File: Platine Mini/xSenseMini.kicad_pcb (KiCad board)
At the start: 2 copper layers, 30 x 20 mm, 25 parts, among them J1 Balancer, J2 Tele_Strom, J3 Serial_AIn, U1 SPX3819 3,3V, U2 ATmega328P-AU, U3 LM4040 2.5

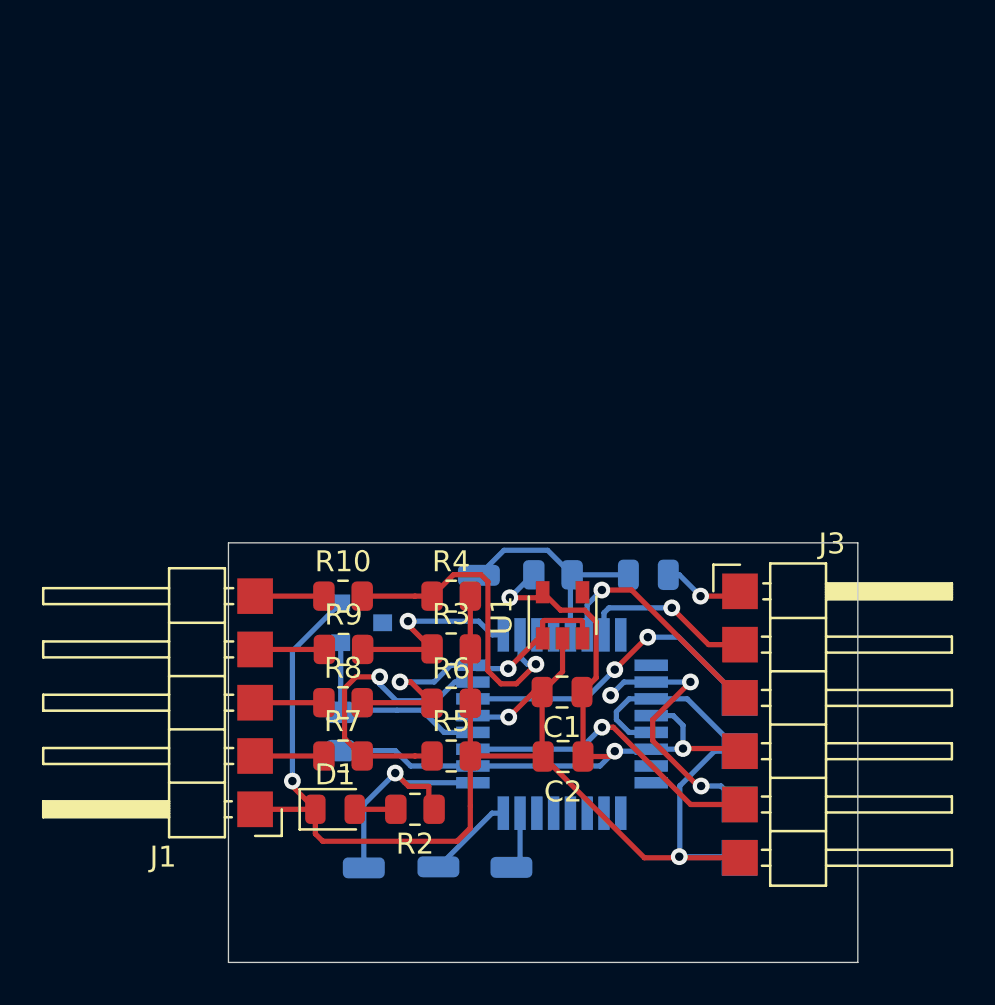
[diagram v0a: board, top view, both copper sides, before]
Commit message: + Schaltplan Mini Update + Komplett neu geroutet und finalisiert
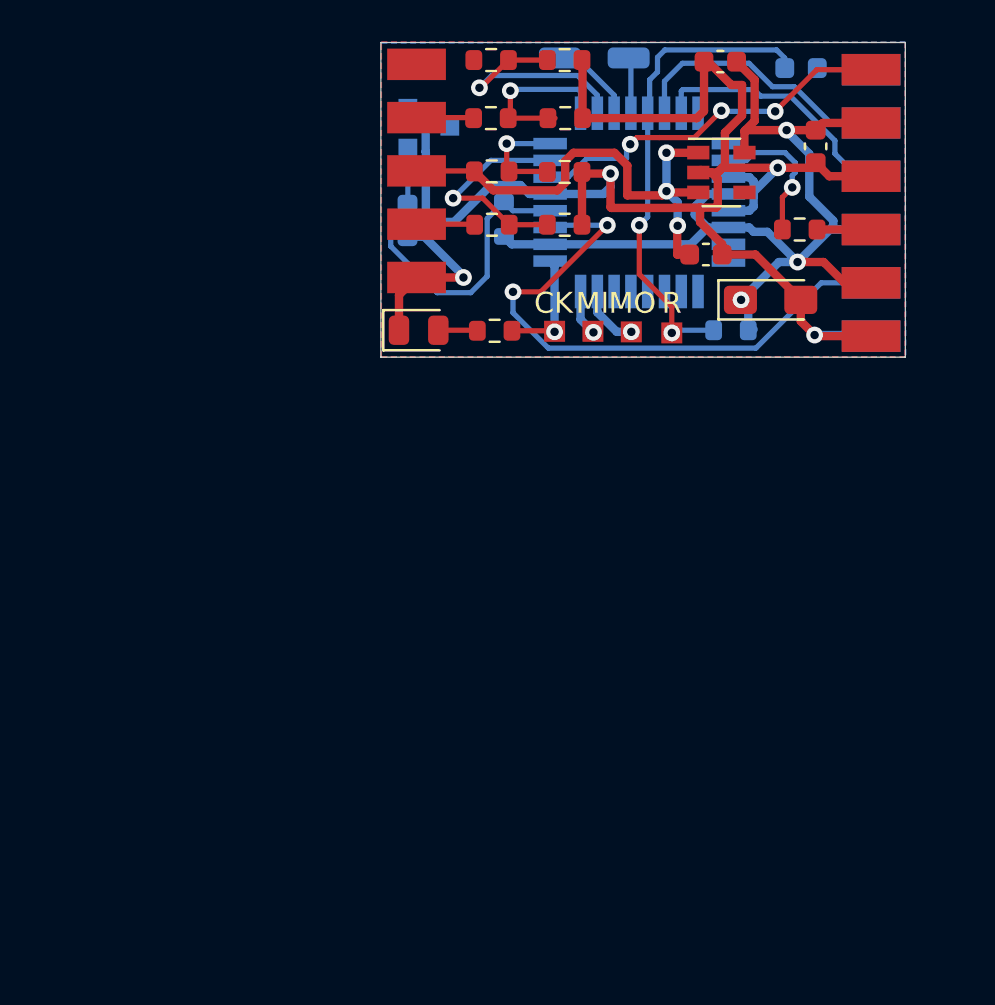
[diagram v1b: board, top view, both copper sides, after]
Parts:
- removed R1: R, Resistor_SMD:R_0805_2012Metric
- removed R2: 1K, Resistor_SMD:R_0805_2012Metric
- added C4: 100nF, Capacitor_SMD:C_0603_1608Metric, B.Cu at (59.3, 32.9)
- added C5: 100nF, Capacitor_SMD:C_0603_1608Metric, F.Cu at (78.8, 29.4)
- added C6: 100nF, Capacitor_SMD:C_0603_1608Metric, B.Cu at (78.1, 25.6)
- added R12: 4,7K, Resistor_SMD:R_0603_1608Metric, F.Cu at (63.3, 30.6)
- added R13: 10K, Resistor_SMD:R_0603_1608Metric, F.Cu at (63.3, 28.0)
- added R14: 12K, Resistor_SMD:R_0603_1608Metric, F.Cu at (63.3, 25.2)
- added TP5: SDA, Connector_Wire:SolderWirePad_1x01_SMD_1x2mm, B.Cu at (66.6, 25.1)
- added TP6: SCL, Connector_Wire:SolderWirePad_1x01_SMD_1x2mm, B.Cu at (69.9, 25.1)
- C1: footprint Capacitor_SMD:C_0805_2012Metric -> Capacitor_SMD:C_0603_1608Metric
- C2: value 10µF -> 100nF; footprint Capacitor_SMD:C_0805_2012Metric -> Capacitor_SMD:C_0603_1608Metric
- C3: value 100nF -> 10µF; footprint Capacitor_SMD:C_0805_2012Metric -> Capacitor_Tantalum_SMD:CP_EIA-3216-10_Kemet-I_Pad1.58x1.35mm_HandSolder; moved to F.Cu
- J1: footprint Connector_PinHeader_2.54mm:PinHeader_1x05_P2.54mm_Horizontal -> xSenseParts:SolderPad_5x
- J2: value Tele_Strom -> Conn_01x06_Male; footprint Connector_PinHeader_2.54mm:PinHeader_1x04_P2.54mm_Horizontal -> xSenseParts:SolderPad_6x; moved to F.Cu
- J3: footprint Connector_PinHeader_2.54mm:PinHeader_1x06_P2.54mm_Horizontal -> xSenseParts:SolderPad_6x; moved to B.Cu
- R10: value 12K -> 2,7K; footprint Resistor_SMD:R_0805_2012Metric -> Resistor_SMD:R_0603_1608Metric
- R11: value 10k -> 1K; footprint Resistor_SMD:R_0805_2012Metric -> Resistor_SMD:R_0603_1608Metric; moved to F.Cu
- R3: value 2,7K -> 560; footprint Resistor_SMD:R_0805_2012Metric -> Resistor_SMD:R_0603_1608Metric; moved to B.Cu
- R4: value 2,7K -> 4K7; footprint Resistor_SMD:R_0805_2012Metric -> Resistor_SMD:R_0603_1608Metric
- R5: value 2,7K -> 1K; footprint Resistor_SMD:R_0805_2012Metric -> Resistor_SMD:R_0603_1608Metric
- R6: value 2,7K -> 10k; footprint Resistor_SMD:R_0805_2012Metric -> Resistor_SMD:R_0603_1608Metric; moved to B.Cu
- R7: value 1K -> 2,7K; footprint Resistor_SMD:R_0805_2012Metric -> Resistor_SMD:R_0603_1608Metric
- R8: value 4,7K -> 2,7K; footprint Resistor_SMD:R_0805_2012Metric -> Resistor_SMD:R_0603_1608Metric
- R9: value 10K -> 2,7K; footprint Resistor_SMD:R_0805_2012Metric -> Resistor_SMD:R_0603_1608Metric
- TP1, TP2, TP3, TP4: footprint Connector_Wire:SolderWirePad_1x01_SMD_1x2mm -> xSenseParts:SolderPad_1x1mm; moved to F.Cu
- U2: value ATmega328P-AU -> LM4040 2.5; footprint Package_QFP:TQFP-32_7x7mm_P0.8mm -> Package_TO_SOT_SMD:SOT-23
- U3: value LM4040 2.5 -> ATmega328P-AU; footprint Package_TO_SOT_SMD:SOT-23 -> Package_QFP:TQFP-32_7x7mm_P0.8mm
- moved C2 34.0 mm to (74.2, 25.3)
- moved J2 31.8 mm to (81.4, 32.1), turned to 270 degrees
- moved J1 31.4 mm to (59.8, 30.5), turned to 90 degrees
- moved U2 29.1 mm to (60.4, 28.4), turned to 0 degrees
- moved R10 27.7 mm to (66.8, 25.2)
- moved R9 27.4 mm to (66.9, 28.0)
- moved R7 27.4 mm to (66.8, 33.1)
- moved R8 27.4 mm to (66.8, 30.6)
- moved TP4 27.1 mm to (66.3, 38.2), turned to 0 degrees
- moved TP3 26.6 mm to (68.2, 38.2), turned to 0 degrees
- moved TP2 26.2 mm to (70.0, 38.2), turned to 0 degrees
- moved R4 24.1 mm to (78.0, 33.3), turned to 180 degrees
- moved U3 24.0 mm to (70.4, 32.0), turned to 180 degrees
- moved D1 23.2 mm to (59.9, 38.1)
- moved U1 22.4 mm to (74.3, 30.6), turned to 0 degrees
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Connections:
- C1 pad 1: +3V3 -> Z2Vcc
- C3 pad 1: ResetSer -> +3V3
- C3 pad 2: Reset -> GND
- J1 pad 3: Net-(J1-Pad3) -> Z2Vcc
- J2 pad 1: GND -> Curr
- J2 pad 2: Tele -> +3V3
- J2 pad 4: Curr -> Tele
- J3 pad 2: Tx -> Rx
- J3 pad 3: Rx -> Tx
- R10 pad 1: Net-(J1-Pad5) -> Z4
- R10 pad 2: Z4 -> GND
- R11 pad 1: Reset -> Net-(J1-Pad2)
- R11 pad 2: +3V3 -> Z1
- R3 pad 1: Z3 -> +3V3
- R3 pad 2: GND -> Net-(C4-Pad1)
- R4 pad 1: Z4 -> Tele
- R4 pad 2: GND -> Net-(R4-Pad2)
- R5 pad 1: Z1 -> CLK
- R5 pad 2: GND -> Net-(D1-Pad2)
- R6 pad 1: Z2 -> Reset
- R6 pad 2: GND -> +3V3
- R7 pad 1: Net-(J1-Pad2) -> Z1
- R7 pad 2: Z1 -> GND
- R8 pad 1: Net-(J1-Pad3) -> Z2
- R8 pad 2: Z2 -> GND
- R9 pad 1: Net-(J1-Pad4) -> Z3
- R9 pad 2: Z3 -> GND
- U1 pad 1: Z2 -> Z2Vcc
- U1 pad 3: Z2 -> Z2Vcc
- U2 pad 1: Net-(U2-Pad1) -> Net-(C4-Pad1)
- U2 pad 2: Tele -> GND
- U2 pad 3: GND -> (no net)
- U3 pad 1: Net-(R1-Pad2) -> Net-(U3-Pad1)
- U3 pad 2: GND -> Net-(R4-Pad2)
- U3 pad 3: (no net) -> GND
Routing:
- net Z2Vcc: track 0.00 -> 24.2 mm, vias 0 -> 3
- net Net-(C4-Pad1): track 0.00 -> 17.2 mm
- net AIn: track 14.7 -> 28.6 mm, vias 1 -> 2
- net +3V3: track 37.3 -> 51.2 mm
- net Reset: track 11.0 -> 23.2 mm, vias 0 -> 2
- net Z2: track 16.4 -> 5.32 mm, vias 2 -> 1
- net Tele: track 13.0 -> 2.58 mm, vias 3 -> 0
- net Net-(R1-Pad2): track 9.47 -> 0.00 mm
- net GND: track 78.2 -> 86.6 mm, vias 3 -> 4
- net Net-(R4-Pad2): track 0.00 -> 7.16 mm, vias 0 -> 1
- net CLK: track 12.2 -> 5.53 mm
- net Z4: track 15.7 -> 10.9 mm
- net Net-(TP5-Pad1): track 0.00 -> 4.25 mm
- net Z1: track 14.3 -> 10.4 mm
- net Tx: track 8.36 -> 12.2 mm, vias 1 -> 0
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- added copper zone on B.Cu, net GND
- added copper zone on F.Cu, net GND
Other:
- board size 30 x 20 mm -> 25 x 15 mm
- board text added: "CK"
- board text added: "MI"
- board text added: "MO"
- board text added: "R"
- board text added: "SCL"
- board text added: "SDA"
- board text added: "xSense DS"
